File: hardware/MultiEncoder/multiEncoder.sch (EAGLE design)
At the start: 51 parts, among them J1 90325-0004, J2 90325-0004, U1 PCA9698DGG-518

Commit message: change to 8 knob per module, 64 knob max
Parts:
- removed MT10, MT11, MT12, MT13, MT14, MT15, MT16, MT9: PEC11R-4215F-S0024, PEC11R-4215F-S0024:PEC11R-4215F-S0024
- removed R10, R11, R12, R13, R14, R15, R16, R17, R18, R19, R20, R21, R22, R23, R24, R25, R26, R27, R28, R29, R30, R31, R32, R7, R8, R9: 10K, rcl:R-US_R0805
- removed U1: PCA9698DGG-518, PCA9698DGG_518:PCA9698DGG-518
- added J3, J4: 90325-0004, 90325-0004:90325-0004
- added U2: MCP23017T-E/SS, MCP23017T-E_SS:MCP23017T-E/SS
- R1, R3, R5: value 10K -> 1
- R2, R4, R6: value 10K -> 0
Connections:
- removed net A10: MT10.A, R20.1, U1.IO2_2
- removed net A11: MT11.A, R22.1, U1.IO2_4
- removed net A12: MT12.A, R24.1, U1.IO2_6
- removed net A13: MT13.A, R26.1, U1.IO3_0
- removed net A14: MT14.A, R28.1, U1.IO3_2
- removed net A15: MT15.A, R30.1, U1.IO3_4
- removed net A16: MT16.A, R32.1, U1.IO3_6
- removed net A9: MT9.A, R18.1, U1.IO2_0
- removed net B10: MT10.B, R19.1, U1.IO2_3
- removed net B11: MT11.B, R21.1, U1.IO2_5
- removed net B12: MT12.B, R23.1, U1.IO2_7
- removed net B13: MT13.B, R25.1, U1.IO3_1
- removed net B14: MT14.B, R27.1, U1.IO3_3
- removed net B15: MT15.B, R29.1, U1.IO3_5
- removed net B16: MT16.B, R31.1, U1.IO3_7
- removed net B9: MT9.B, R17.1, U1.IO2_1
- new net ADR0: R1.2, R2.1, U2.A0
- new net ADR1: R3.2, R4.1, U2.A1
- new net ADR2: R5.2, R6.1, U2.A2
- net A1: now also U2.GPA0; no longer R1.1, U1.IO0_0
- net A2: now also U2.GPA2; no longer R4.1, U1.IO0_2
- net A3: now also U2.GPA4; no longer R6.1, U1.IO0_4
- net A4: now also U2.GPA6; no longer R8.1, U1.IO0_6
- net A5: now also U2.GPB0; no longer R10.1, U1.IO1_0
- net A6: now also U2.GPB2; no longer R12.1, U1.IO1_2
- net A7: now also U2.GPB4; no longer U1.IO1_4
- net A7\: no longer R14.1
- net A8: now also U2.GPB6; no longer R16.1, U1.IO1_6
- net B1: now also U2.GPA1; no longer R2.1, U1.IO0_1
- net B2: now also U2.GPA3; no longer R3.1, U1.IO0_3
- net B3: now also U2.GPA5; no longer R5.1, U1.IO0_5
- net B4: now also U2.GPA7; no longer R7.1, U1.IO0_7
- net B5: now also U2.GPB1; no longer R9.1, U1.IO1_1
- net B6: now also U2.GPB3; no longer R11.1, U1.IO1_3
- net B7: now also U2.GPB5; no longer R13.1, U1.IO1_5
- net B8: now also U2.GPB7; no longer R15.1, U1.IO1_7
- net GND: now also J3.2, J4.2, R2.2, R4.2, R6.2, U2.VSS; no longer MT10.COM, MT10.SHIELD, MT11.COM, MT11.SHIELD, MT12.COM, MT12.SHIELD, MT13.COM, MT13.SHIELD, MT14.COM, MT14.SHIELD, MT15.COM, MT15.SHIELD, MT16.COM, MT16.SHIELD, MT9.COM, MT9.SHIELD
- net SCL: now also J3.3, J4.3, U2.SCK
- net SDA: now also J3.4, J4.4, U2.SDA
- net VCC: now also J3.1, J4.1, R1.1, R3.1, R5.1, U2.!RESET, U2.VDD; no longer R1.2, R10.2, R11.2, R12.2, R13.2, R14.2, R15.2, R16.2, R17.2, R18.2, R19.2, R2.2, R20.2, R21.2, R22.2, R23.2, R24.2, R25.2, R26.2, R27.2, R28.2, R29.2, R3.2, R30.2, R31.2, R32.2, R4.2, R5.2, R6.2, R7.2, R8.2, R9.2
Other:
- note added: "These are meant to be globbed over by the user, but only one per pin, either the vcc or gnd"
- moved on the sheet: R1, R2, R3, R4, R5, R6

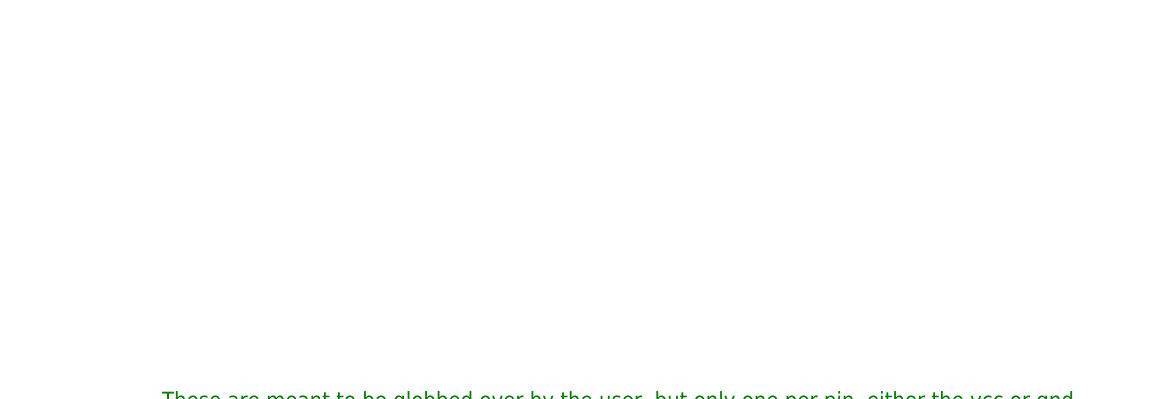
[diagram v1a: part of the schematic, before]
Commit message: Parts are placed, add ploygons and optional i2c line pullups
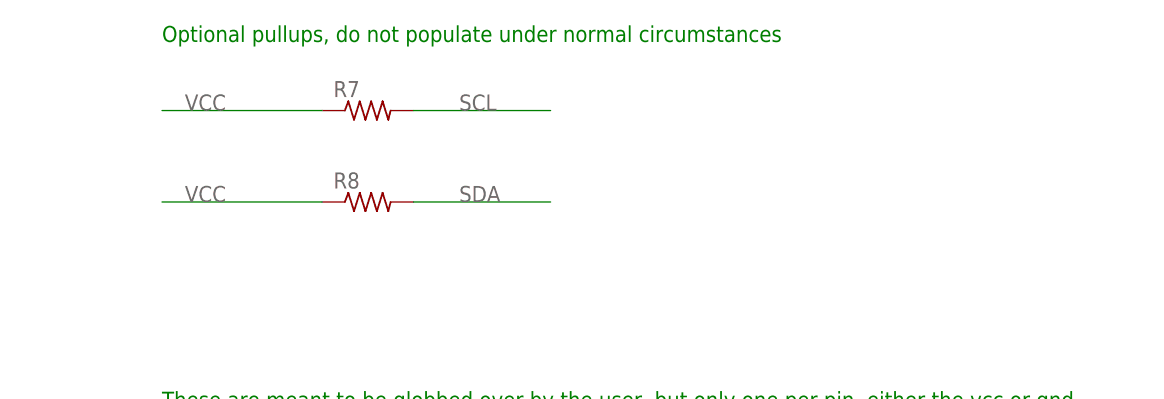
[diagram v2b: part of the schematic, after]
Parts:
- added R7, R8: 1K, rcl:R-US_R0805
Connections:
- net SCL: now also R7.2
- net SDA: now also R8.2
- net VCC: now also R7.1, R8.1
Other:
- note added: "Optional pullups, do not populate under normal circumstances"
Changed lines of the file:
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@@
 <part name="R5" library="rcl" library_urn="urn:adsk.eagle:library:334" deviceset="R-US_" device="R0805" package3d_urn="urn:adsk.eagle:package:23553/2" value="1"/>
 <part name="R6" library="rcl" library_urn="urn:adsk.eagle:library:334" deviceset="R-US_" device="R0805" package3d_urn="urn:adsk.eagle:package:23553/2" value="0"/>
+<part name="R7" library="rcl" library_urn="urn:adsk.eagle:library:334" deviceset="R-US_" device="R0805" package3d_urn="urn:adsk.eagle:package:23553/2" value="1K"/>
+<part name="R8" library="rcl" library_urn="urn:adsk.eagle:library:334" deviceset="R-US_" device="R0805" package3d_urn="urn:adsk.eagle:package:23553/2" value="1K"/>
 </parts>
 <sheets>
@@
 <plain>
 <text x="114.3" y="22.86" size="1.778" layer="91">These are meant to be globbed over by the user, but only one per pin, either the vcc or gnd</text>
+<text x="114.3" y="63.5" size="1.778" layer="91">Optional pullups, do not populate under normal circumstances</text>
 </plain>
 <instances>
@@
 <attribute name="NAME" x="161.29" y="1.4986" size="1.778" layer="95"/>
 <attribute name="VALUE" x="161.29" y="-3.302" size="1.778" layer="96"/>
+</instance>
+<instance part="R7" gate="G$1" x="137.16" y="55.88" smashed="yes">
+<attribute name="NAME" x="133.35" y="57.3786" size="1.778" layer="95"/>
+</instance>
+<instance part="R8" gate="G$1" x="137.16" y="45.72" smashed="yes">
+<attribute name="NAME" x="133.35" y="47.2186" size="1.778" layer="95"/>
 </instance>
 </instances>
@@
 <label x="121.92" y="-38.1" size="1.778" layer="95"/>
 </segment>
+<segment>
+<wire x1="114.3" y1="55.88" x2="132.08" y2="55.88" width="0.1524" layer="91"/>
+<label x="116.84" y="55.88" size="1.778" layer="95"/>
+<pinref part="R7" gate="G$1" pin="1"/>
+</segment>
+<segment>
+<wire x1="114.3" y1="45.72" x2="132.08" y2="45.72" width="0.1524" layer="91"/>
+<label x="116.84" y="45.72" size="1.778" layer="95"/>
+<pinref part="R8" gate="G$1" pin="1"/>
+</segment>
 </net>
 <net name="SCL" class="0">
@@
 <label x="15.24" y="25.4" size="1.778" layer="95"/>
 </segment>
+<segment>
+<pinref part="R7" gate="G$1" pin="2"/>
+<wire x1="142.24" y1="55.88" x2="157.48" y2="55.88" width="0.1524" layer="91"/>
+<label x="147.32" y="55.88" size="1.778" layer="95"/>
+</segment>
 </net>
 <net name="SDA" class="0">
@@
 <label x="15.24" y="22.86" size="1.778" layer="95"/>
 </segment>
+<segment>
+<pinref part="R8" gate="G$1" pin="2"/>
+<wire x1="142.24" y1="45.72" x2="157.48" y2="45.72" width="0.1524" layer="91"/>
+<label x="147.32" y="45.72" size="1.778" layer="95"/>
+</segment>
 </net>

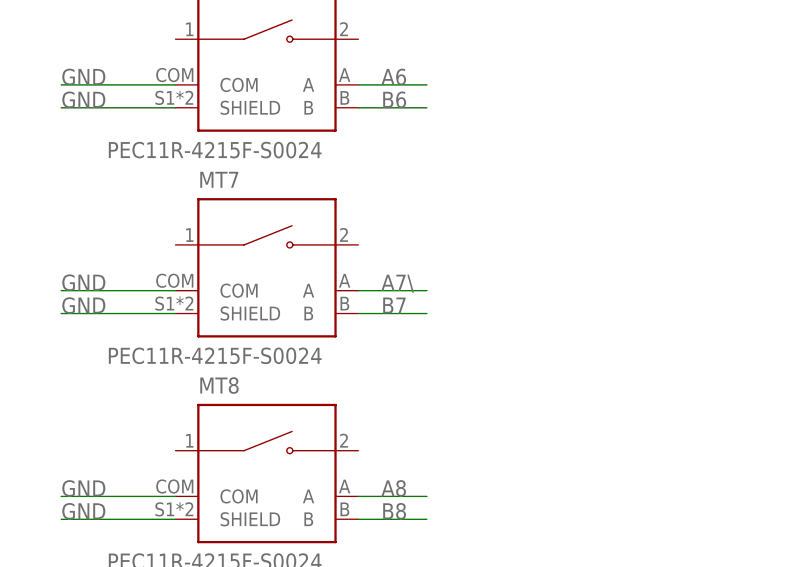
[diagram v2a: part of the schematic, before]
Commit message: All signals routed, ERC and DRC passes, just need to check footprints really
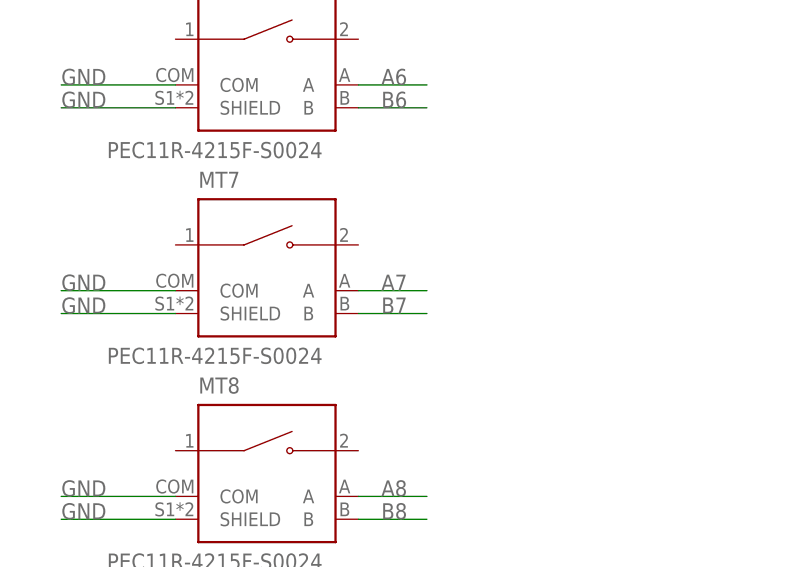
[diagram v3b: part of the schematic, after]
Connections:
- removed net A7\: MT7.A
- net A7: now also MT7.A
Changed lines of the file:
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@@
-</segment>
-</net>
-<net name="A7\" class="0">
-<segment>
-<pinref part="MT7" gate="G$1" pin="A"/>
-<wire x1="88.9" y1="-134.62" x2="81.28" y2="-134.62" width="0.1524" layer="91"/>
-<label x="83.82" y="-134.62" size="1.778" layer="95"/>
 </segment>
 </net>
@@
 <pinref part="U2" gate="G$1" pin="GPB4"/>
 </segment>
+<segment>
+<pinref part="MT7" gate="G$1" pin="A"/>
+<wire x1="88.9" y1="-134.62" x2="81.28" y2="-134.62" width="0.1524" layer="91"/>
+<label x="83.82" y="-134.62" size="1.778" layer="95"/>
+</segment>
 </net>
 <net name="ADR2" class="0">
@@
 </sheet>
 </sheets>
+<errors>
+</errors>
 </schematic>
 </drawing>

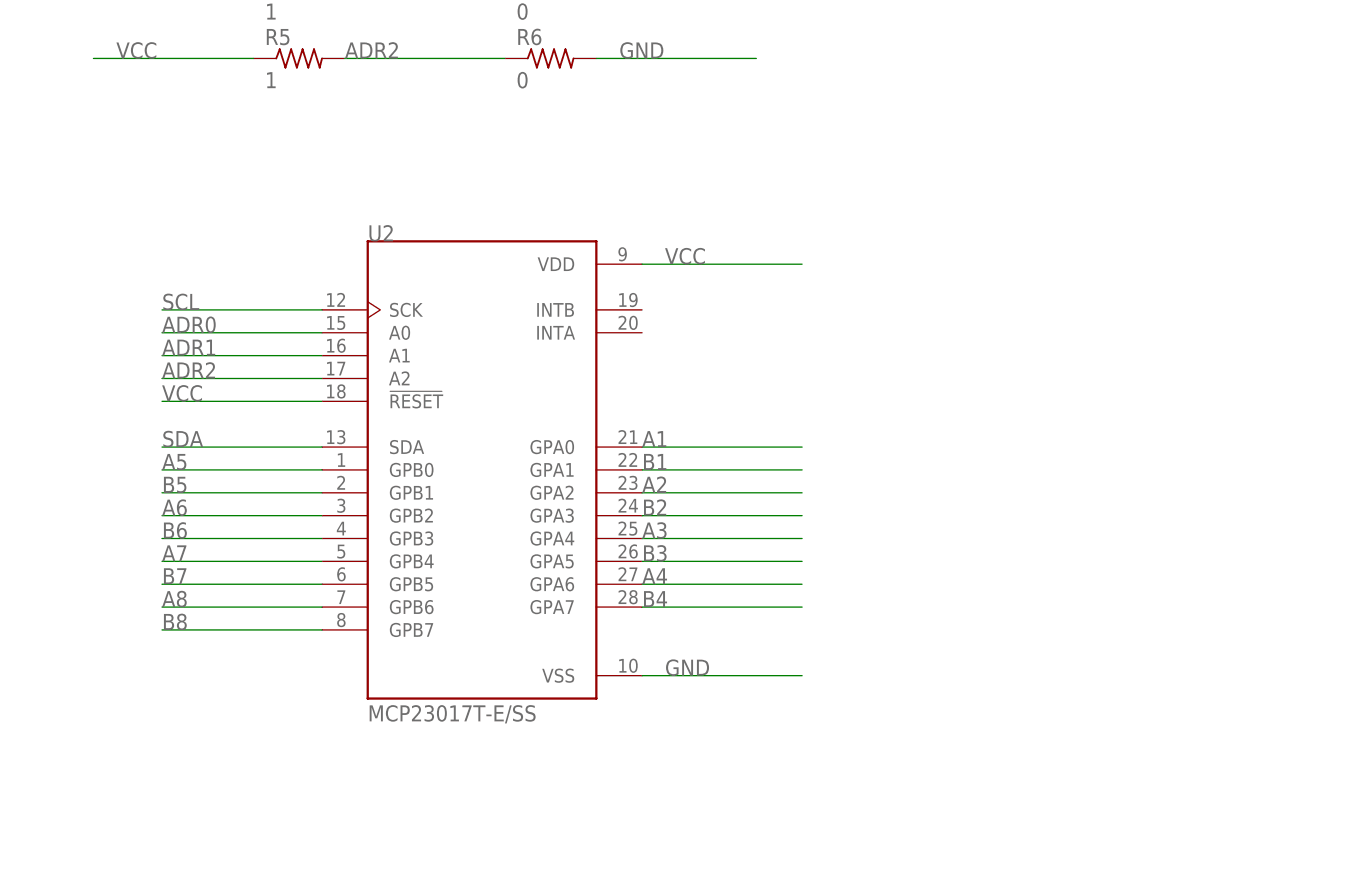
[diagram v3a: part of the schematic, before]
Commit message: Switch to a dip package for the ioexpander chip, re route signals
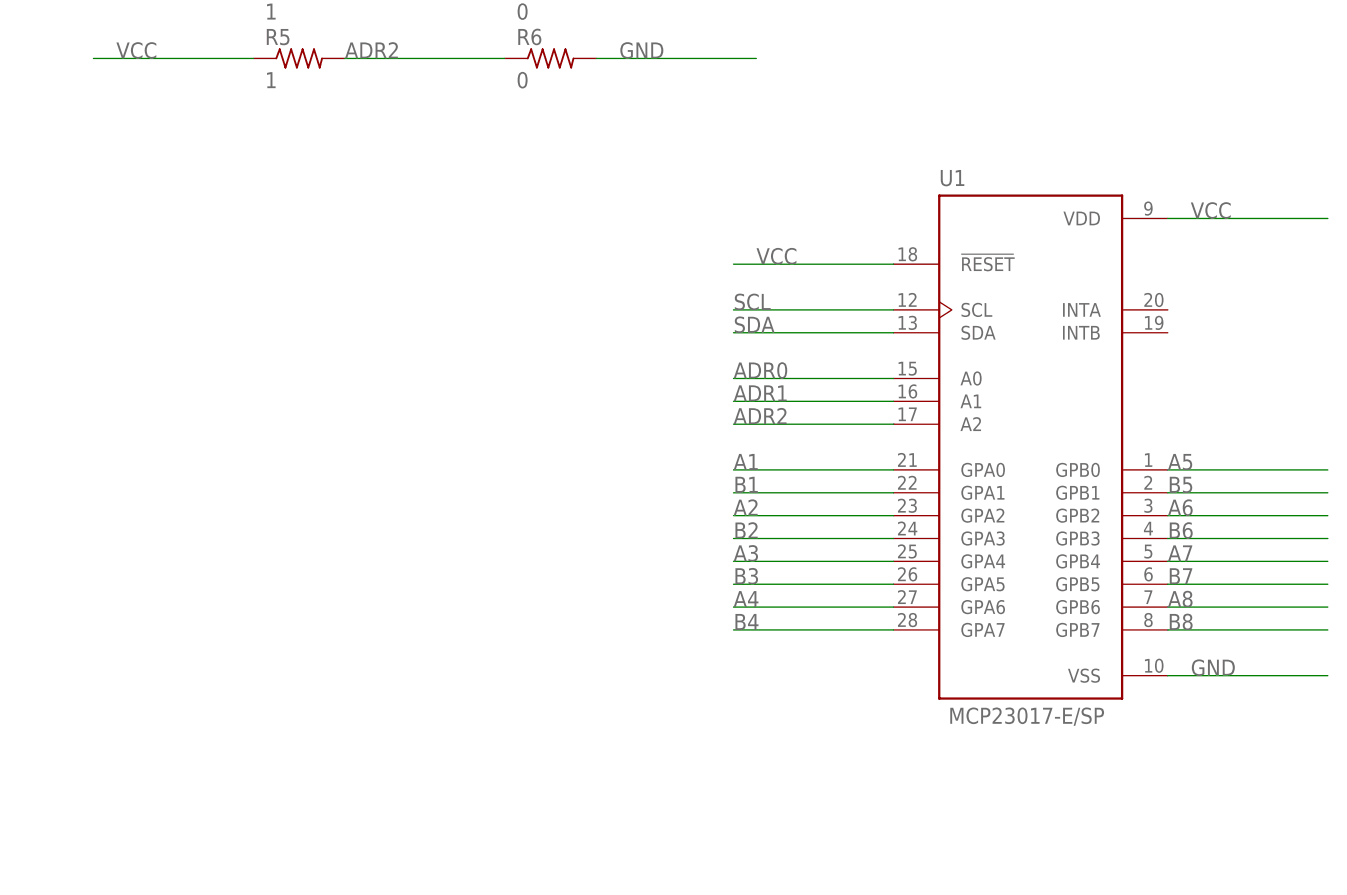
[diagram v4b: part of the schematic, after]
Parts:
- removed U2: MCP23017T-E/SS, MCP23017T-E_SS:MCP23017T-E/SS
- added U1: MCP23017-E/SP, MCP23017-E_SP:MCP23017-E/SP
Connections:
- net A1: now also U1.GPA0; no longer U2.GPA0
- net A2: now also U1.GPA2; no longer U2.GPA2
- net A3: now also U1.GPA4; no longer U2.GPA4
- net A4: now also U1.GPA6; no longer U2.GPA6
- net A5: now also U1.GPB0; no longer U2.GPB0
- net A6: now also U1.GPB2; no longer U2.GPB2
- net A7: now also U1.GPB4; no longer U2.GPB4
- net A8: now also U1.GPB6; no longer U2.GPB6
- net ADR0: now also U1.A0; no longer U2.A0
- net ADR1: now also U1.A1; no longer U2.A1
- net ADR2: now also U1.A2; no longer U2.A2
- net B1: now also U1.GPA1; no longer U2.GPA1
- net B2: now also U1.GPA3; no longer U2.GPA3
- net B3: now also U1.GPA5; no longer U2.GPA5
- net B4: now also U1.GPA7; no longer U2.GPA7
- net B5: now also U1.GPB1; no longer U2.GPB1
- net B6: now also U1.GPB3; no longer U2.GPB3
- net B7: now also U1.GPB5; no longer U2.GPB5
- net B8: now also U1.GPB7; no longer U2.GPB7
- net GND: now also U1.VSS; no longer U2.VSS
- net SCL: now also U1.SCL; no longer U2.SCK
- net SDA: now also U1.SDA; no longer U2.SDA
- net VCC: now also U1.!RESET, U1.VDD; no longer U2.!RESET, U2.VDD

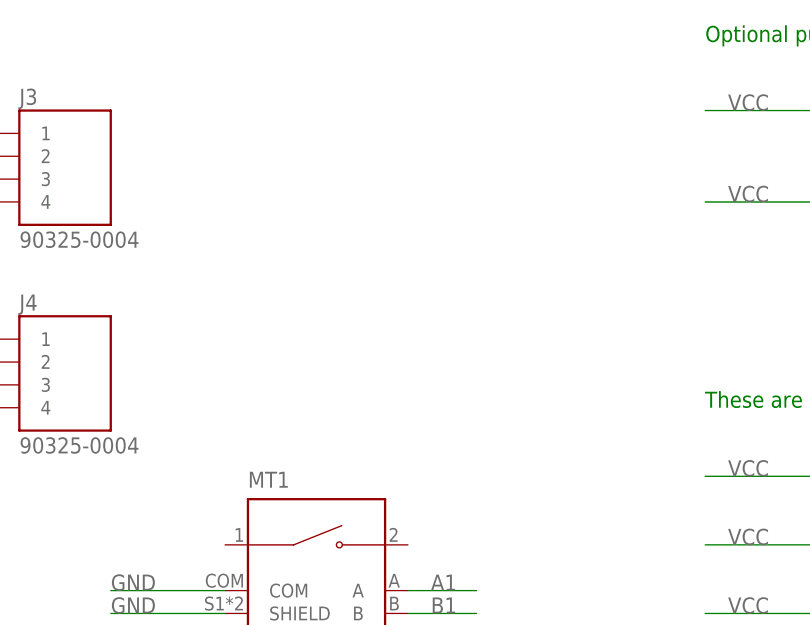
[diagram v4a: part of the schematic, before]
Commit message: add vertical connection option
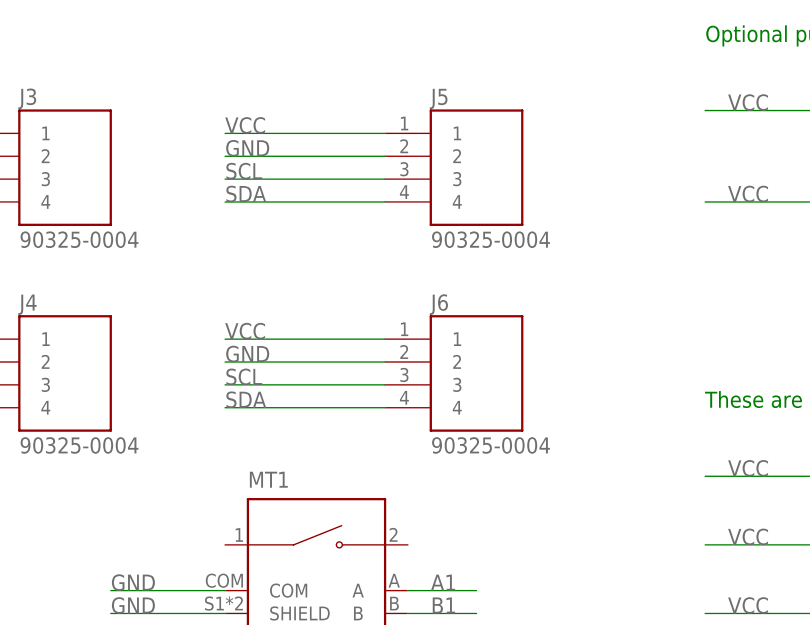
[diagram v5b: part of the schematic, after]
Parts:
- added J5, J6: 90325-0004, 90325-0004:90325-0004
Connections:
- net GND: now also J5.2, J6.2
- net SCL: now also J5.3, J6.3
- net SDA: now also J5.4, J6.4
- net VCC: now also J5.1, J6.1
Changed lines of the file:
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@@
 <part name="R8" library="rcl" library_urn="urn:adsk.eagle:library:334" deviceset="R-US_" device="R0805" package3d_urn="urn:adsk.eagle:package:23553/2" value="1K"/>
 <part name="U1" library="MCP23017-E_SP" deviceset="MCP23017-E/SP" device=""/>
+<part name="J5" library="90325-0004" deviceset="90325-0004" device=""/>
+<part name="J6" library="90325-0004" deviceset="90325-0004" device=""/>
 </parts>
 <sheets>
@@
 <attribute name="VALUE" x="209.291509375" y="-73.9279" size="1.77886875" layer="96"/>
 </instance>
+<instance part="J5" gate="G$1" x="88.9" y="50.8" smashed="yes">
+<attribute name="NAME" x="83.82" y="56.515" size="1.778" layer="95" ratio="10" rot="SR0"/>
+<attribute name="VALUE" x="83.82" y="40.64" size="1.778" layer="96" ratio="10" rot="SR0"/>
+</instance>
+<instance part="J6" gate="G$1" x="88.9" y="27.94" smashed="yes">
+<attribute name="NAME" x="83.82" y="33.655" size="1.778" layer="95" ratio="10" rot="SR0"/>
+<attribute name="VALUE" x="83.82" y="17.78" size="1.778" layer="96" ratio="10" rot="SR0"/>
+</instance>
 </instances>
 <busses>
@@
 <pinref part="U1" gate="G$1" pin="VSS"/>
 </segment>
+<segment>
+<pinref part="J5" gate="G$1" pin="2"/>
+<wire x1="78.74" y1="50.8" x2="60.96" y2="50.8" width="0.1524" layer="91"/>
+<label x="60.96" y="50.8" size="1.778" layer="95"/>
+</segment>
+<segment>
+<pinref part="J6" gate="G$1" pin="2"/>
+<wire x1="78.74" y1="27.94" x2="60.96" y2="27.94" width="0.1524" layer="91"/>
+<label x="60.96" y="27.94" size="1.778" layer="95"/>
+</segment>
 </net>
 <net name="VCC" class="0">
@@
 <pinref part="U1" gate="G$1" pin="VDD"/>
 </segment>
+<segment>
+<pinref part="J5" gate="G$1" pin="1"/>
+<wire x1="78.74" y1="53.34" x2="60.96" y2="53.34" width="0.1524" layer="91"/>
+<label x="60.96" y="53.34" size="1.778" layer="95"/>
+</segment>
+<segment>
+<pinref part="J6" gate="G$1" pin="1"/>
+<wire x1="78.74" y1="30.48" x2="60.96" y2="30.48" width="0.1524" layer="91"/>
+<label x="60.96" y="30.48" size="1.778" layer="95"/>
+</segment>
 </net>
 <net name="SCL" class="0">
@@
 <pinref part="U1" gate="G$1" pin="SCL"/>
 </segment>
+<segment>
+<pinref part="J5" gate="G$1" pin="3"/>
+<wire x1="78.74" y1="48.26" x2="60.96" y2="48.26" width="0.1524" layer="91"/>
+<label x="60.96" y="48.26" size="1.778" layer="95"/>
+</segment>
+<segment>
+<pinref part="J6" gate="G$1" pin="3"/>
+<wire x1="78.74" y1="25.4" x2="60.96" y2="25.4" width="0.1524" layer="91"/>
+<label x="60.96" y="25.4" size="1.778" layer="95"/>
+</segment>
 </net>
 <net name="SDA" class="0">
@@
 <pinref part="U1" gate="G$1" pin="SDA"/>
 </segment>
+<segment>
+<pinref part="J5" gate="G$1" pin="4"/>
+<wire x1="78.74" y1="45.72" x2="60.96" y2="45.72" width="0.1524" layer="91"/>
+<label x="60.96" y="45.72" size="1.778" layer="95"/>
+</segment>
+<segment>
+<pinref part="J6" gate="G$1" pin="4"/>
+<wire x1="78.74" y1="22.86" x2="60.96" y2="22.86" width="0.1524" layer="91"/>
+<label x="60.96" y="22.86" size="1.778" layer="95"/>
+</segment>
 </net>
